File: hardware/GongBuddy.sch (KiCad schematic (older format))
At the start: 51 parts, among them J1 USB_B_Mini, J3 2908-05WB-MG, J4 Conn_01x15, J5 Conn_01x02, J7 Conn_Coaxial, J8 Conn_01x15, Q1 MMBT3904, U1 TPS7A19, U2 USBLC6-2SC6, U3 MCP73831T-2ACI_OT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

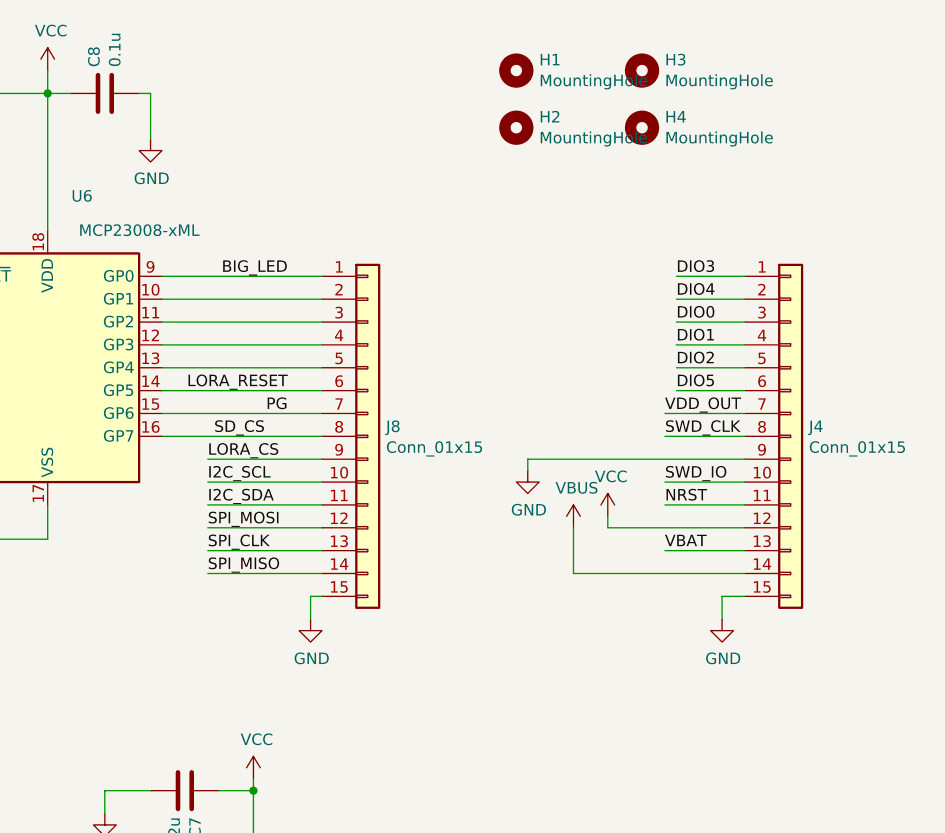
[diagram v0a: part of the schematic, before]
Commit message: Refactor board to a 4 layer.
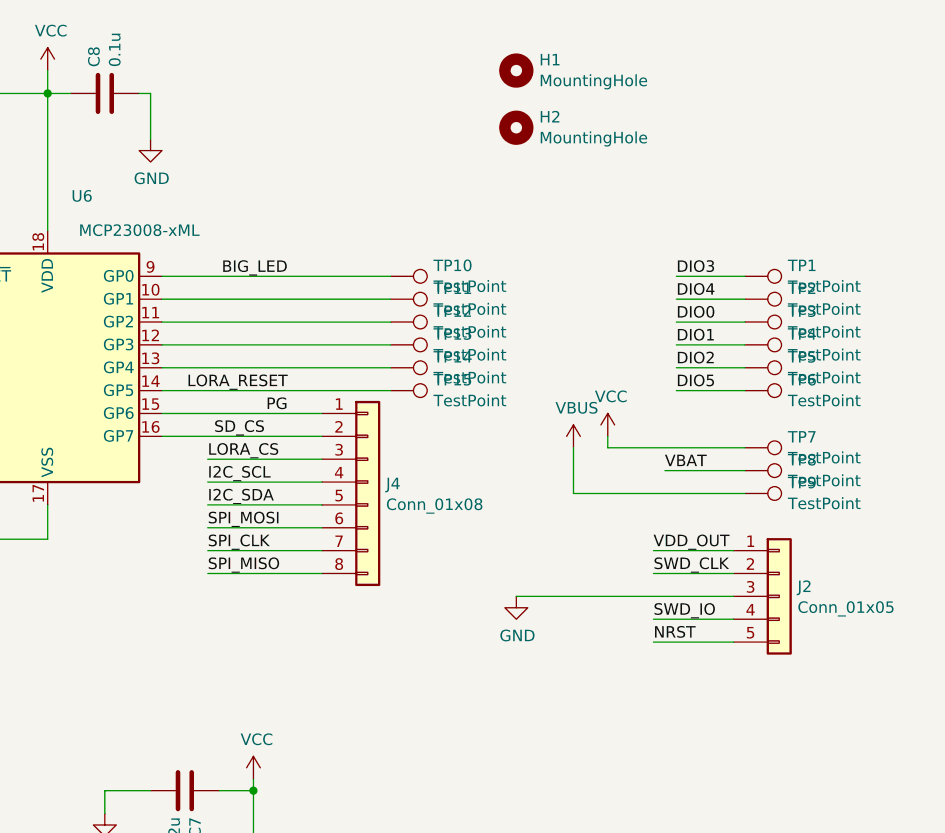
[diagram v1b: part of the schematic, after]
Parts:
- removed H3, H4: MountingHole, MountingHole:MountingHole_2.7mm_M2.5, symbol Mechanical:MountingHole
- removed J4, J8: Conn_01x15, Connector_PinHeader_2.54mm:PinHeader_1x15_P2.54mm_Vertical, symbol Connector_Generic:Conn_01x15
- added J2: Conn_01x05, Connector_PinHeader_2.54mm:PinHeader_1x05_P2.54mm_Vertical, symbol Connector_Generic:Conn_01x05
- added J4: Conn_01x08, Connector_PinHeader_2.54mm:PinHeader_1x08_P2.54mm_Vertical, symbol Connector_Generic:Conn_01x08
- added TP1, TP10, TP11, TP12, TP13, TP14, TP15, TP2, TP3, TP4, TP5, TP6, TP7, TP8, TP9: TestPoint, TestPoint:TestPoint_Pad_D1.5mm, symbol Connector:TestPoint
- H1, H2: footprint MountingHole:MountingHole_2.7mm_M2.5 -> MountingHole:MountingHole_4mm
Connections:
- net BIG_LED: now also TP10.1
- net DIO0: now also TP3.1
- net DIO1: now also TP4.1
- net DIO2: now also TP5.1
- net DIO3: now also TP1.1
- net DIO4: now also TP2.1
- net DIO5: now also TP6.1
- net GND: now also J2.3 (Pin_3)
- net I2C_SCL: now also J4.4 (Pin_4)
- net I2C_SDA: now also J4.5 (Pin_5)
- net LORA_CS: now also J4.3 (Pin_3)
- net LORA_RESET: now also TP15.1
- net NRST: now also J2.5 (Pin_5)
- net PG: now also J4.1 (Pin_1)
- net SD_CS: now also J4.2 (Pin_2)
- net SPI_CLK: now also J4.7 (Pin_7)
- net SPI_MISO: now also J4.8 (Pin_8)
- net SPI_MOSI: now also J4.6 (Pin_6)
- net SWD_CLK: now also J2.2 (Pin_2)
- net SWD_IO: now also J2.4 (Pin_4)
- net VBAT: now also TP8.1
- net VBUS: now also TP9.1
- net VCC: now also TP7.1
- net VDD_OUT: now also J2.1 (Pin_1)
- net at U6.10 (GP1): now also TP11.1
- net at U6.11 (GP2): now also TP12.1
- net at U6.12 (GP3): now also TP13.1
- net at U6.13 (GP4): now also TP14.1

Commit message: Updated part numbers.
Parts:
- C1, C4, C7: Digi-Key_PN (none) -> 445-14428-1-ND
- C2, C3, C8: Digi-Key_PN (none) -> GRM188R71C104KA01D
- C5, C6: Digi-Key_PN (none) -> 490-12737-1-ND
- C9: Digi-Key_PN (none) -> 1276-3364-1-ND
- D1: Digi-Key_PN (none) -> VLCS5830-ND
- D2, D3, D4, D5, D6, D7, D8, D9: Digi-Key_PN (none) -> 475-2709-1-ND
- J5: Digi-Key_PN (none) -> ‎455-1704-ND‎
- J7: Digi-Key_PN (none) -> CON-SMA-EDGE-S-ND
- Q1: Digi-Key_PN (none) -> MMBT3904FSCT-ND
- R1, R3: Digi-Key_PN (none) -> 408-1912-1-ND
- R10, R11, R12, R13, R14, R15, R16, R17: Digi-Key_PN (none) -> P330GCT-ND
- R2, R4: Digi-Key_PN (none) -> P0.0GCT-ND
- R5: Digi-Key_PN (none) -> P10KYCT
- R6: Digi-Key_PN (none) -> 541-15.8KCCT-ND
- R7: Digi-Key_PN (none) -> 311-11.0KCRCT-ND
- R9: Digi-Key_PN (none) -> 311-2.00KHRCT-ND
- U1: Digi-Key_PN (none) -> 296-45026-1-ND
- U2: Digi-Key_PN (none) -> 497-5235-2-ND; Digikey 497-5235-2-ND -> (none)
- U5: Digi-Key_PN (none) -> RFM95W-915S2-ND
- U6: Digi-Key_PN (none) -> MCP23008T-E/MLCT-ND
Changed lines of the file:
@@
 F 2 "RF_Module:HOPERF_RFM9XW_SMD" H 5350 6600 50  0001 C CNN
 F 3 "https://www.hoperf.com/data/upload/portal/20181127/5bfcbea20e9ef.pdf" H 5350 6600 50  0001 C CNN
+F 4 "RFM95W-915S2-ND" H 8650 4950 50  0001 C CNN "Digi-Key_PN"
 	1    8650 4950
 	1    0    0    -1
@@
 F 2 "Package_TO_SOT_SMD:SOT-23" H 1700 7025 50  0001 L CIN
 F 3 "https://www.onsemi.com/pub/Collateral/2N3903-D.PDF" H 1500 7100 50  0001 L CNN
+F 4 "MMBT3904FSCT-ND" H 1500 7100 50  0001 C CNN "Digi-Key_PN"
 	1    1500 7100
 	1    0    0    -1
@@
 F 2 "LED_THT:LED_D1.8mm_W1.8mm_H2.4mm_Horizontal_O1.27mm_Z1.6mm" H 1600 6250 50  0001 C CNN
 F 3 "~" H 1600 6250 50  0001 C CNN
+F 4 "VLCS5830-ND" H 1600 6250 50  0001 C CNN "Digi-Key_PN"
 	1    1600 6250
 	0    -1   -1   0
@@
 F 2 "Capacitor_SMD:C_0603_1608Metric" H 3688 1350 50  0001 C CNN
 F 3 "~" H 3650 1500 50  0001 C CNN
+F 4 "490-12737-1-ND" H 3650 1500 50  0001 C CNN "Digi-Key_PN"
 	1    3650 1500
 	1    0    0    -1
@@
 F 2 "Resistor_SMD:R_0603_1608Metric" V 4080 1950 50  0001 C CNN
 F 3 "~" H 4150 1950 50  0001 C CNN
+F 4 "311-2.00KHRCT-ND" H 4150 1950 50  0001 C CNN "Digi-Key_PN"
 	1    4150 1950
 	1    0    0    -1
@@
 F 2 "LED_SMD:LED_0603_1608Metric" H 6150 1250 50  0001 C CNN
 F 3 "~" H 6150 1250 50  0001 C CNN
+F 4 "475-2709-1-ND" H 6150 1250 50  0001 C CNN "Digi-Key_PN"
 	1    6150 1250
 	0    -1   -1   0
@@
 F 2 "Resistor_SMD:R_0603_1608Metric" V 6080 1650 50  0001 C CNN
 F 3 "~" H 6150 1650 50  0001 C CNN
+F 4 "P330GCT-ND" H 6150 1650 50  0001 C CNN "Digi-Key_PN"
 	1    6150 1650
 	1    0    0    -1
@@
 F 2 "Resistor_SMD:R_0603_1608Metric" V 6080 2100 50  0001 C CNN
 F 3 "~" H 6150 2100 50  0001 C CNN
+F 4 "P330GCT-ND" H 6150 2100 50  0001 C CNN "Digi-Key_PN"
 	1    6150 2100
 	1    0    0    -1
@@
 F 2 "LED_SMD:LED_0603_1608Metric" H 6150 2500 50  0001 C CNN
 F 3 "~" H 6150 2500 50  0001 C CNN
+F 4 "475-2709-1-ND" H 6150 2500 50  0001 C CNN "Digi-Key_PN"
 	1    6150 2500
 	0    -1   -1   0
@@
 F 2 "Capacitor_SMD:C_0603_1608Metric" H 5638 1550 50  0001 C CNN
 F 3 "~" H 5600 1700 50  0001 C CNN
+F 4 "490-12737-1-ND" H 5600 1700 50  0001 C CNN "Digi-Key_PN"
 	1    5600 1700
 	1    0    0    -1
@@
 F 2 "Connector_JST:JST_PH_B2B-PH-K_1x02_P2.00mm_Vertical" H 1900 2650 50  0001 C CNN
 F 3 "~" H 1900 2650 50  0001 C CNN
+F 4 "‎455-1704-ND‎" H 1900 2650 50  0001 C CNN "Digi-Key_PN"
 	1    1900 2650
 	1    0    0    -1
@@
 F 2 "Package_TO_SOT_SMD:SOT-23-6" H 1950 1500 50  0001 C CNN
 F 3 "" H 1950 1500 50  0001 C CNN
-F 4 "497-5235-2-ND" H 1950 1500 50  0001 C CNN "Digikey"
+F 4 "497-5235-2-ND" H 1950 1500 50  0001 C CNN "Digi-Key_PN"
 	1    1950 1500
 	-1   0    0    -1
@@
 F 2 "Package_SON:HVSON-8-1EP_3x3mm_P0.65mm_EP1.6x2.4mm" H 1800 4000 60  0001 C CNN
 F 3 "" H 1800 4000 60  0001 C CNN
+F 4 "296-45026-1-ND" H 1800 4000 50  0001 C CNN "Digi-Key_PN"
 	1    1800 4000
 	1    0    0    -1
@@
 F 2 "Resistor_SMD:R_0603_1608Metric" V 3030 3800 50  0001 C CNN
 F 3 "~" H 3100 3800 50  0001 C CNN
+F 4 "541-15.8KCCT-ND" H 3100 3800 50  0001 C CNN "Digi-Key_PN"
 	1    3100 3800
 	1    0    0    -1
@@
 F 2 "Capacitor_SMD:C_1206_3216Metric" H 688 4000 50  0001 C CNN
 F 3 "~" H 650 4150 50  0001 C CNN
+F 4 "445-14428-1-ND" H 650 4150 50  0001 C CNN "Digi-Key_PN"
 	1    650  4150
 	1    0    0    -1
@@
 F 2 "Capacitor_SMD:C_0603_1608Metric" H 988 4450 50  0001 C CNN
 F 3 "~" H 950 4600 50  0001 C CNN
+F 4 "GRM188R71C104KA01D" H 950 4600 50  0001 C CNN "Digi-Key_PN"
 	1    950  4600
 	1    0    0    -1
@@
 F 2 "Resistor_SMD:R_0603_1608Metric" V 3030 4250 50  0001 C CNN
 F 3 "~" H 3100 4250 50  0001 C CNN
+F 4 "311-11.0KCRCT-ND" H 3100 4250 50  0001 C CNN "Digi-Key_PN"
 	1    3100 4250
 	1    0    0    -1
@@
 F 2 "Resistor_SMD:R_0603_1608Metric" V 2530 3650 50  0001 C CNN
 F 3 "~" H 2600 3650 50  0001 C CNN
+F 4 "P10KYCT" H 2600 3650 50  0001 C CNN "Digi-Key_PN"
 	1    2600 3650
 	1    0    0    -1
@@
 F 2 "Capacitor_SMD:C_1206_3216Metric" H 3638 3900 50  0001 C CNN
 F 3 "~" H 3600 4050 50  0001 C CNN
+F 4 "445-14428-1-ND" H 3600 4050 50  0001 C CNN "Digi-Key_PN"
 	1    3600 4050
 	1    0    0    -1
@@
 F 2 "Capacitor_SMD:C_0603_1608Metric" H 8388 3750 50  0001 C CNN
 F 3 "~" H 8350 3900 50  0001 C CNN
+F 4 "445-14428-1-ND" H 8350 3900 50  0001 C CNN "Digi-Key_PN"
 	1    8350 3900
 	0    1    1    0
@@
 F 2 "Package_DFN_QFN:QFN-20-1EP_4x4mm_P0.5mm_EP2.7x2.7mm" H 7750 1000 50  0001 C CNN
 F 3 "http://ww1.microchip.com/downloads/en/DeviceDoc/MCP23008-MCP23S08-Data-Sheet-20001919F.pdf" H 9050 850 50  0001 C CNN
+F 4 "MCP23008T-E/MLCT-ND" H 7750 2050 50  0001 C CNN "Digi-Key_PN"
 	1    7750 2050
 	1    0    0    -1
@@
 F 2 "Capacitor_SMD:C_0603_1608Metric" H 8038 700 50  0001 C CNN
 F 3 "~" H 8000 850 50  0001 C CNN
+F 4 "GRM188R71C104KA01D" H 8000 850 50  0001 C CNN "Digi-Key_PN"
 	1    8000 850
 	0    -1   -1   0
@@
 F 2 "Resistor_SMD:R_1206_3216Metric" V 1530 6650 50  0001 C CNN
 F 3 "~" H 1600 6650 50  0001 C CNN
+F 4 "408-1912-1-ND" H 1600 6650 50  0001 C CNN "Digi-Key_PN"
 	1    1600 6650
 	1    0    0    -1
@@
 F 2 "Capacitor_SMD:C_0603_1608Metric" H 3538 6850 50  0001 C CNN
 F 3 "~" H 3500 7000 50  0001 C CNN
+F 4 "GRM188R71C104KA01D" H 3500 7000 50  0001 C CNN "Digi-Key_PN"
 	1    3500 7000
 	1    0    0    -1
@@
 F 2 "Resistor_SMD:R_0603_1608Metric" V 1130 5850 50  0001 C CNN
 F 3 "~" H 1200 5850 50  0001 C CNN
+F 4 "P0.0GCT-ND" H 1200 5850 50  0001 C CNN "Digi-Key_PN"
 	1    1200 5850
 	1    0    0    -1
@@
 F 2 "Resistor_SMD:R_0603_1608Metric" V 1830 5850 50  0001 C CNN
 F 3 "~" H 1900 5850 50  0001 C CNN
+F 4 "P0.0GCT-ND" H 1900 5850 50  0001 C CNN "Digi-Key_PN"
 	1    1900 5850
 	1    0    0    -1
@@
 F 2 "LED_SMD:LED_0603_1608Metric" H 9250 5900 50  0001 C CNN
 F 3 "~" H 9250 5900 50  0001 C CNN
+F 4 "475-2709-1-ND" H 9250 5900 50  0001 C CNN "Digi-Key_PN"
 	1    9250 5900
 	0    -1   -1   0
@@
 F 2 "Resistor_SMD:R_0603_1608Metric" V 9180 5550 50  0001 C CNN
 F 3 "~" H 9250 5550 50  0001 C CNN
+F 4 "P330GCT-ND" H 9250 5550 50  0001 C CNN "Digi-Key_PN"
 	1    9250 5550
 	1    0    0    -1
@@
 F 2 "LED_SMD:LED_0603_1608Metric" H 9600 5900 50  0001 C CNN
 F 3 "~" H 9600 5900 50  0001 C CNN
+F 4 "475-2709-1-ND" H 9600 5900 50  0001 C CNN "Digi-Key_PN"
 	1    9600 5900
 	0    -1   -1   0
@@
 F 2 "Resistor_SMD:R_0603_1608Metric" V 9530 5550 50  0001 C CNN
 F 3 "~" H 9600 5550 50  0001 C CNN
+F 4 "P330GCT-ND" H 9600 5550 50  0001 C CNN "Digi-Key_PN"
 	1    9600 5550
 	1    0    0    -1
@@
 F 2 "LED_SMD:LED_0603_1608Metric" H 9900 5900 50  0001 C CNN
 F 3 "~" H 9900 5900 50  0001 C CNN
+F 4 "475-2709-1-ND" H 9900 5900 50  0001 C CNN "Digi-Key_PN"
 	1    9900 5900
 	0    -1   -1   0
@@
 F 2 "Resistor_SMD:R_0603_1608Metric" V 9830 5550 50  0001 C CNN
 F 3 "~" H 9900 5550 50  0001 C CNN
+F 4 "P330GCT-ND" H 9900 5550 50  0001 C CNN "Digi-Key_PN"
 	1    9900 5550
 	1    0    0    -1
@@
 F 2 "LED_SMD:LED_0603_1608Metric" H 10200 5900 50  0001 C CNN
 F 3 "~" H 10200 5900 50  0001 C CNN
+F 4 "475-2709-1-ND" H 10200 5900 50  0001 C CNN "Digi-Key_PN"
 	1    10200 5900
 	0    -1   -1   0
@@
 F 2 "Resistor_SMD:R_0603_1608Metric" V 10130 5550 50  0001 C CNN
 F 3 "~" H 10200 5550 50  0001 C CNN
+F 4 "P330GCT-ND" H 10200 5550 50  0001 C CNN "Digi-Key_PN"
 	1    10200 5550
 	1    0    0    -1
@@
 F 2 "LED_SMD:LED_0603_1608Metric" H 10500 5900 50  0001 C CNN
 F 3 "~" H 10500 5900 50  0001 C CNN
+F 4 "475-2709-1-ND" H 10500 5900 50  0001 C CNN "Digi-Key_PN"
 	1    10500 5900
 	0    -1   -1   0
@@
 F 2 "Resistor_SMD:R_0603_1608Metric" V 10430 5550 50  0001 C CNN
 F 3 "~" H 10500 5550 50  0001 C CNN
+F 4 "P330GCT-ND" H 10500 5550 50  0001 C CNN "Digi-Key_PN"
 	1    10500 5550
 	1    0    0    -1
@@
 F 2 "LED_SMD:LED_0603_1608Metric" H 10800 5900 50  0001 C CNN
 F 3 "~" H 10800 5900 50  0001 C CNN
+F 4 "475-2709-1-ND" H 10800 5900 50  0001 C CNN "Digi-Key_PN"
 	1    10800 5900
 	0    -1   -1   0
@@
 F 2 "Resistor_SMD:R_0603_1608Metric" V 10730 5550 50  0001 C CNN
 F 3 "~" H 10800 5550 50  0001 C CNN
+F 4 "P330GCT-ND" H 10800 5550 50  0001 C CNN "Digi-Key_PN"
 	1    10800 5550
 	1    0    0    -1
@@
 F 2 "Connector_Coaxial:SMA_Amphenol_132289_EdgeMount" H 10500 4250 50  0001 C CNN
 F 3 " ~" H 10500 4250 50  0001 C CNN
+F 4 "CON-SMA-EDGE-S-ND" H 10500 4250 50  0001 C CNN "Digi-Key_PN"
 	1    10500 4250
 	1    0    0    -1
@@
 F 2 "Capacitor_SMD:CP_Elec_3x5.3" H 2500 5850 50  0001 C CNN
 F 3 "~" H 2500 5850 50  0001 C CNN
+F 4 "1276-3364-1-ND" H 2500 5850 50  0001 C CNN "Digi-Key_PN"
 	1    2500 5850
 	1    0    0    -1
@@
 F 2 "Resistor_SMD:R_1206_3216Metric" V 1280 6650 50  0001 C CNN
 F 3 "~" H 1350 6650 50  0001 C CNN
+F 4 "408-1912-1-ND" H 1350 6650 50  0001 C CNN "Digi-Key_PN"
 	1    1350 6650
 	1    0    0    -1
